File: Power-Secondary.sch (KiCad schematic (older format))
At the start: 57 parts, among them J1 AUXBatteryConn, J10 BPS +12V, J2 BATT DISCNCT, J3 BPS MAIN SUPPLY, J4 JUMP START, J5 HORN CTRL, J6 DRV FAN CTRL, J7 HORN +12V, J8 DRIVER FAN +12V, J9 RADIOS +12V, K1 G5Q-1, K2 G5Q-1, K3 G5Q-1, SW1 Batt Check, SW2 BPS PWR CHECK, SW3 RADIO PWR CHECK

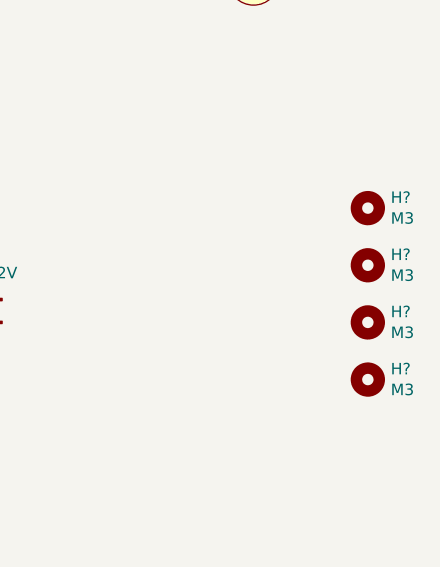
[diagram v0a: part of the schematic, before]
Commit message: Updates schematics to match secondary power board v1.1
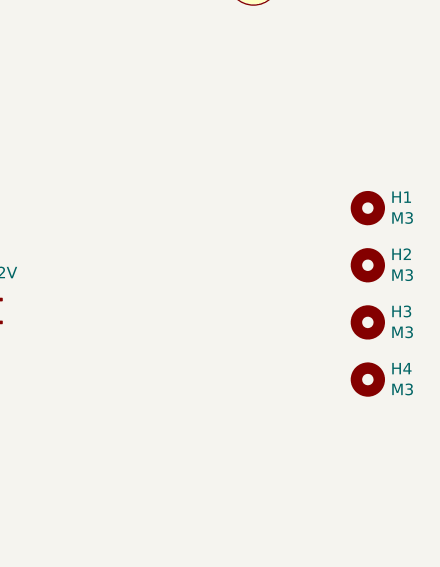
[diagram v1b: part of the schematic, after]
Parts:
- gave numbers to parts that had none: 4
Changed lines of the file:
@@
 	4000 7600 4000 7500
 $Comp
-L Mechanical:MountingHole H?
+L Mechanical:MountingHole H1
 U 1 1 5F59BD9F
 P 9000 5000
-F 0 "H?" H 9100 5046 50  0000 L CNN
+F 0 "H1" H 9100 5046 50  0000 L CNN
 F 1 "M3" H 9100 4955 50  0000 L CNN
 F 2 "MountingHole:MountingHole_3mm" H 9000 5000 50  0001 C CNN
@@
 $EndComp
 $Comp
-L Mechanical:MountingHole H?
+L Mechanical:MountingHole H2
 U 1 1 5F59D039
 P 9000 5250
-F 0 "H?" H 9100 5296 50  0000 L CNN
+F 0 "H2" H 9100 5296 50  0000 L CNN
 F 1 "M3" H 9100 5205 50  0000 L CNN
 F 2 "MountingHole:MountingHole_3mm" H 9000 5250 50  0001 C CNN
@@
 $EndComp
 $Comp
-L Mechanical:MountingHole H?
+L Mechanical:MountingHole H3
 U 1 1 5F59D410
 P 9000 5500
-F 0 "H?" H 9100 5546 50  0000 L CNN
+F 0 "H3" H 9100 5546 50  0000 L CNN
 F 1 "M3" H 9100 5455 50  0000 L CNN
 F 2 "MountingHole:MountingHole_3mm" H 9000 5500 50  0001 C CNN
@@
 $EndComp
 $Comp
-L Mechanical:MountingHole H?
+L Mechanical:MountingHole H4
 U 1 1 5F59D7C1
 P 9000 5750
-F 0 "H?" H 9100 5796 50  0000 L CNN
+F 0 "H4" H 9100 5796 50  0000 L CNN
 F 1 "M3" H 9100 5705 50  0000 L CNN
 F 2 "MountingHole:MountingHole_3mm" H 9000 5750 50  0001 C CNN
